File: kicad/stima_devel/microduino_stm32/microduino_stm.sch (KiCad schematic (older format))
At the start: 24 parts, among them IC1 STM32F103CBT6, IC2 LP2985, Y1 8M, Y2 32.768K

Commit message: Update schematic and testing partial routing
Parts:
- removed BUT1: KMR211GLFS, Button_Switch_SMD:SW_Push_1P1T_NO_CK_KMR2, symbol microduino_stm32-eagle-import:BUTTON-KMR241GLFS
- removed IC2: LP2985, Package_TO_SOT_SMD:SOT-23-5_HandSoldering, symbol microduino_stm32-eagle-import:LP2985
- removed KEY1: KEY-TES-018, Button_Switch_SMD:SW_SPST_EVQP7A, symbol microduino_stm32-eagle-import:KEY-TES-018
- removed LED1: BLUE, LED_SMD:LED_0805_2012Metric_Pad1.15x1.40mm_HandSolder, symbol microduino_stm32-eagle-import:LED0805
- removed R2: 1K, Resistor_SMD:R_1206_3216Metric_Pad1.30x1.75mm_HandSolder, symbol microduino_stm32-eagle-import:RESISTOR0603-RES
- removed R6: 47k, Resistor_SMD:R_1206_3216Metric_Pad1.30x1.75mm_HandSolder, symbol microduino_stm32-eagle-import:RESISTOR0603-RES
- removed R7: 10k, Resistor_SMD:R_1206_3216Metric_Pad1.30x1.75mm_HandSolder, symbol microduino_stm32-eagle-import:RESISTOR0603-RES
- removed R8, R9: 22, Resistor_SMD:R_1206_3216Metric_Pad1.30x1.75mm_HandSolder, symbol microduino_stm32-eagle-import:RESISTOR0603-RES
- removed U$2: NPN-2P, Package_TO_SOT_SMD:SOT-23-6_Handsoldering, symbol microduino_stm32-eagle-import:NPN-2P
- removed USB1: MICRO_USB, Connector_USB:USB_Micro-B_GCT_USB3076-30-A, symbol microduino_stm32-eagle-import:MICRO_USB
- removed Y2: 32.768K, Crystal:Crystal_SMD_3215-2Pin_3.2x1.5mm, symbol microduino_stm32-eagle-import:CRYSTAL-32.768K-3215
- added D2: D, Diode_SMD:D_0805_2012Metric, symbol Device:D
- added J1, J3: Conn_01x01, TestPoint:TestPoint_Pad_1.0x1.0mm, symbol Connector_Generic:Conn_01x01
- added J2: USB_B_Micro, Connector_USB:USB_Micro-B_GCT_USB3076-30-A, symbol Connector:USB_B_Micro
- added SW1: SW_Push, Button_Switch_SMD:SW_SPST_B3U-3000P, symbol Switch:SW_Push
- added SW2: SW_Push, Button_Switch_SMD:SW_Push_1P1T_NO_CK_KMR2, symbol Switch:SW_Push
- added Y2: 32.768KHz, Crystal:Crystal_SMD_EuroQuartz_EQ161-2Pin_3.2x1.5mm_HandSoldering, symbol Device:Crystal
- C1, F1: footprint Capacitor_SMD:C_1206_3216Metric_Pad1.33x1.80mm_HandSolder -> Capacitor_SMD:C_0805_2012Metric
- C6, C7: footprint Capacitor_SMD:C_1206_3216Metric_Pad1.33x1.80mm_HandSolder -> Capacitor_SMD:C_0603_1608Metric
- R1: value 1.5k -> 22; footprint Resistor_SMD:R_1206_3216Metric_Pad1.30x1.75mm_HandSolder -> Capacitor_SMD:C_0805_2012Metric
- R10, R4: footprint Resistor_SMD:R_1206_3216Metric_Pad1.30x1.75mm_HandSolder -> Capacitor_SMD:C_0805_2012Metric
- R3: value 36k -> 22; footprint Resistor_SMD:R_1206_3216Metric_Pad1.30x1.75mm_HandSolder -> Capacitor_SMD:C_0805_2012Metric
- R5: value 1k -> 1.5k; footprint Resistor_SMD:R_1206_3216Metric_Pad1.30x1.75mm_HandSolder -> Capacitor_SMD:C_0805_2012Metric
- Y1: footprint Crystal:Resonator_SMD_muRata_CSTxExxV-3Pin_3.0x1.1mm_HandSoldering -> Crystal:Resonator_SMD_muRata_CSTxExxV-3Pin_3.0x1.1mm
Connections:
- net labels removed: 32, N$13, USB_5V
- wire segments 161 -> 127
- no-connect marks 10 -> 8
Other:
- moved on the sheet: C7

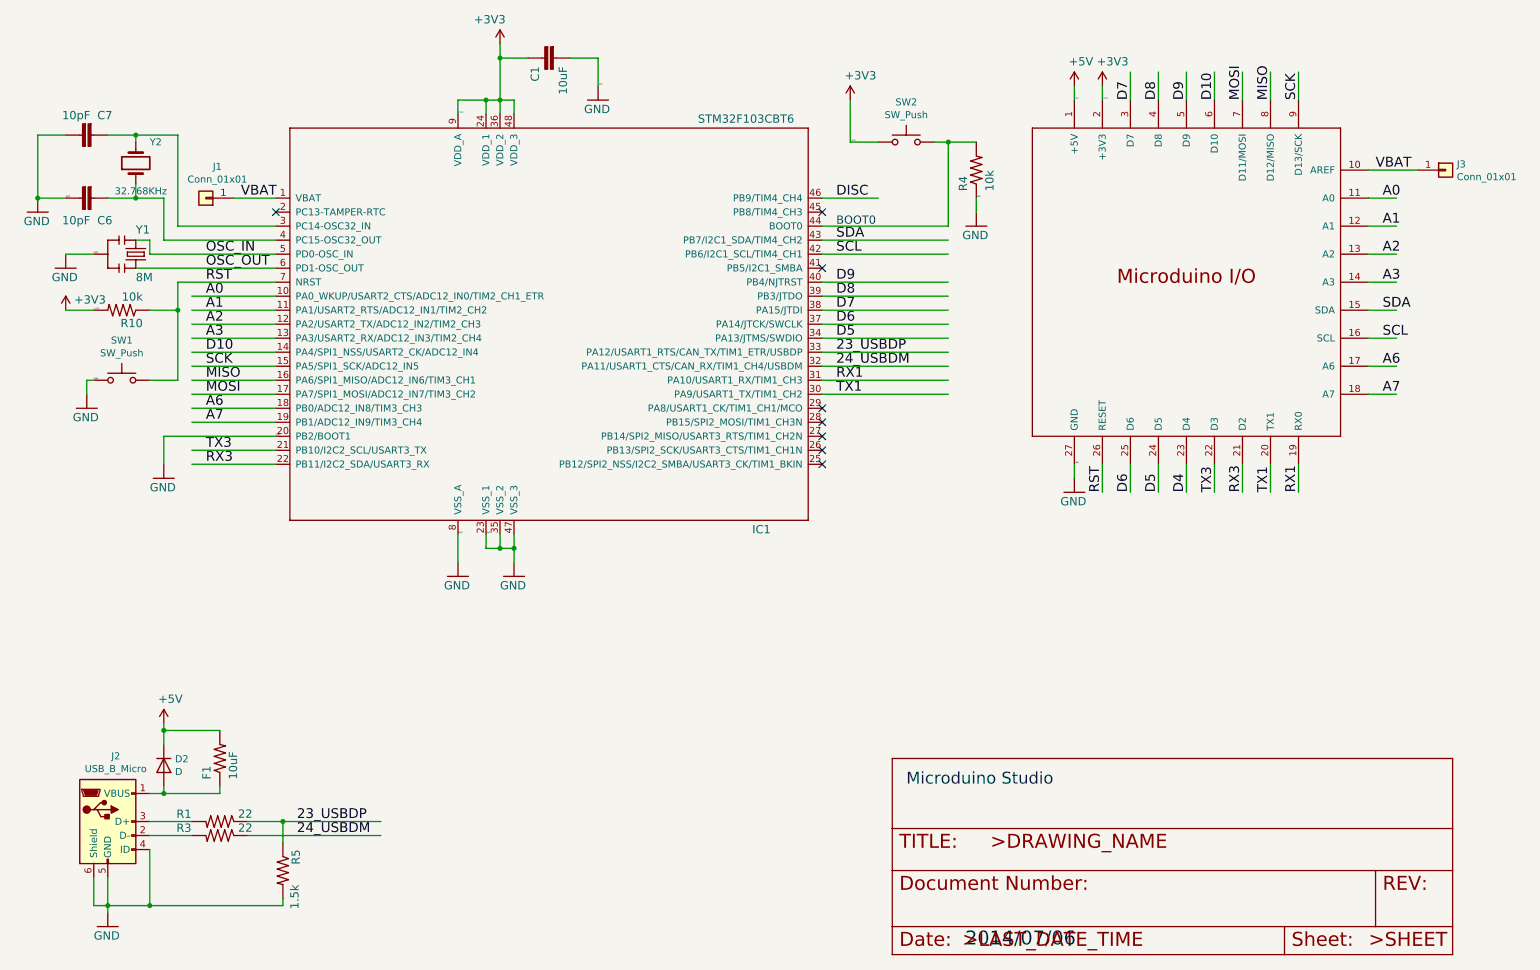
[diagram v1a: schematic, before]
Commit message: complete redraw pcb after error assignement microduino component
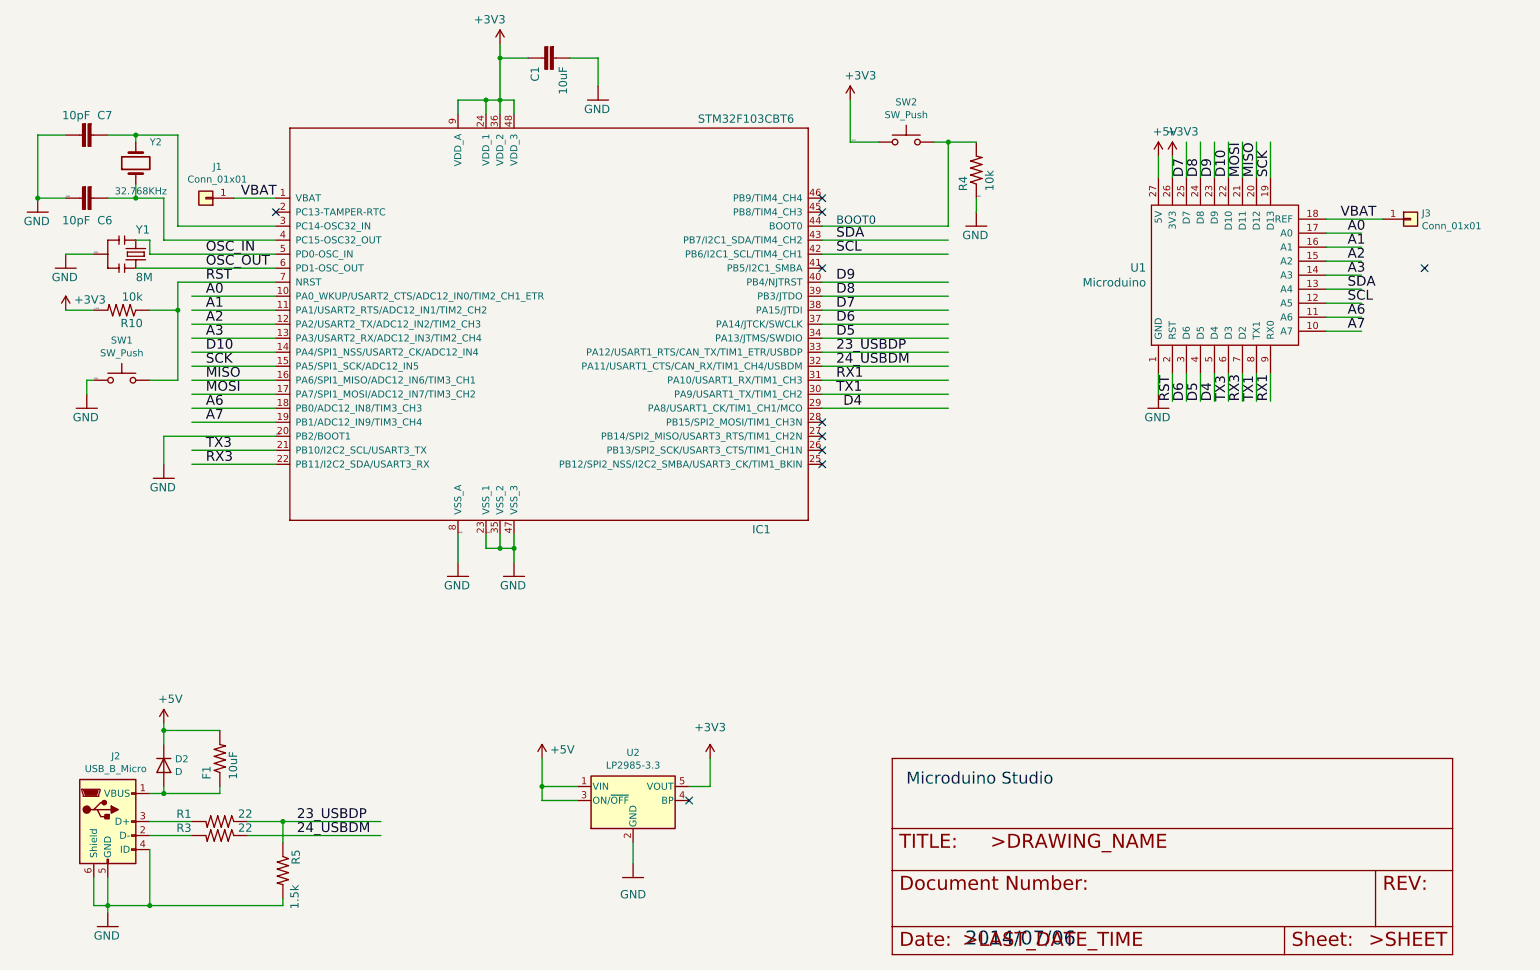
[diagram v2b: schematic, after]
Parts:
- removed U$4: MICRDUINO-PIN_NORMAL, Microduino:microduino, symbol microduino_stm32-eagle-import:MICRDUINO-PIN_NORMAL
- added U1: Microduino, Microduino:microduino, symbol microduino:Microduino
- added U2: LP2985-3.3, Package_TO_SOT_SMD:SOT-23-5, symbol Regulator_Linear:LP2985-3.3
- Y2: footprint Crystal:Crystal_SMD_EuroQuartz_EQ161-2Pin_3.2x1.5mm_HandSoldering -> Crystal:Crystal_SMD_EuroQuartz_EQ161-2Pin_3.2x1.5mm
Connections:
- net labels removed: DISC
- wire segments 127 -> 134
- no-connect marks 8 -> 10
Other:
- moved on the sheet: J3

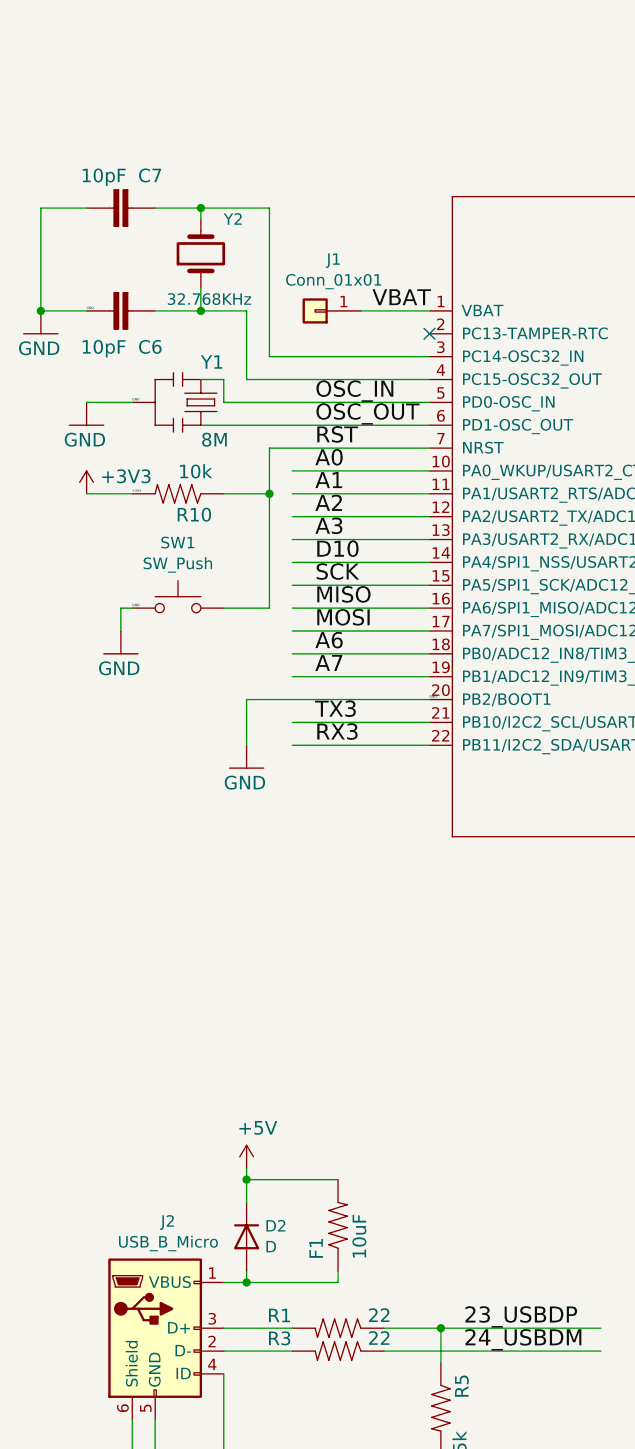
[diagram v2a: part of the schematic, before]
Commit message: update schematic
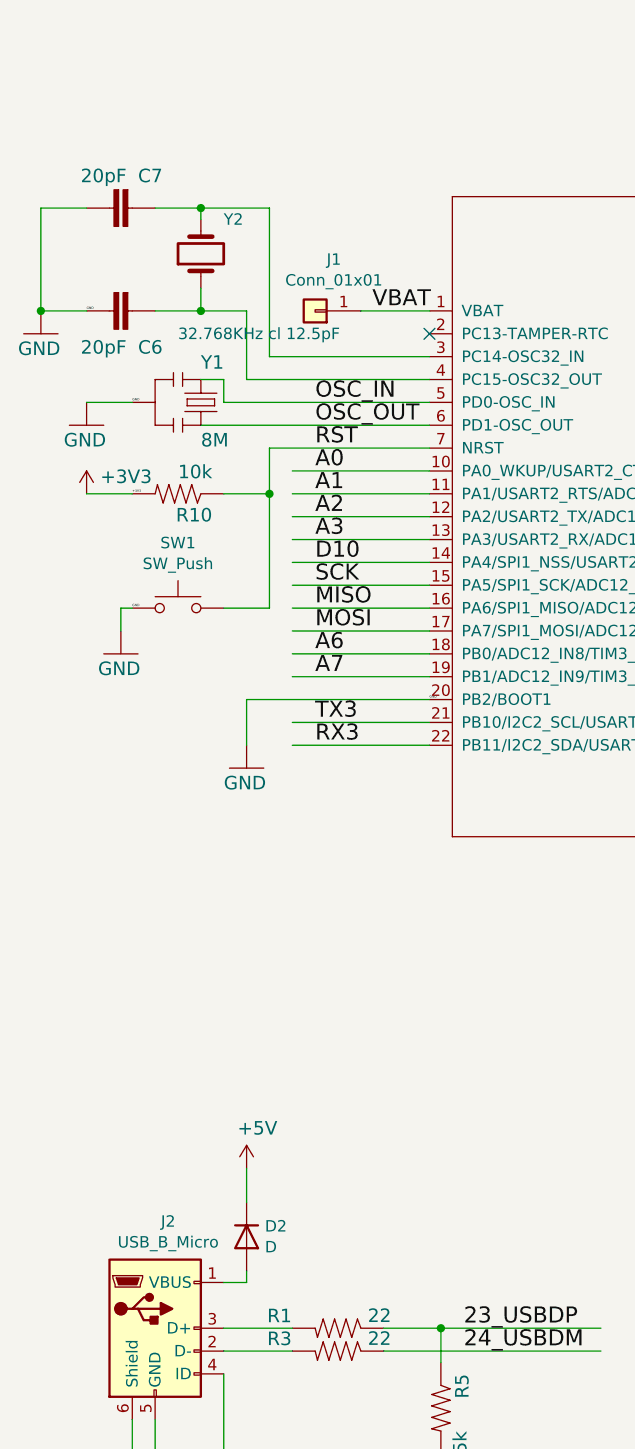
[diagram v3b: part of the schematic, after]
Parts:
- removed F1: 10uF, Capacitor_SMD:C_0805_2012Metric, symbol microduino_stm32-eagle-import:RESISTOR0805-RES
- C6, C7: value 10pF -> 20pF
- R1, R10, R3, R4, R5: footprint Capacitor_SMD:C_0805_2012Metric -> Resistor_SMD:R_0805_2012Metric
- Y2: value 32.768KHz -> 32.768KHz cl 12.5pF
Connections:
- wire segments 134 -> 130
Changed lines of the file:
@@
 F 0 "R4" H 7750 1859 59  0000 L BNN
 F 1 "10k" H 7750 1670 59  0000 L BNN
-F 2 "Capacitor_SMD:C_0805_2012Metric" H 7900 1800 50  0001 C CNN
+F 2 "Resistor_SMD:R_0805_2012Metric" H 7900 1800 50  0001 C CNN
 F 3 "" H 7900 1800 50  0001 C CNN
 	1    7900 1800
@@
 F 0 "R10" H 1650 2859 59  0000 L BNN
 F 1 "10k" H 1650 2670 59  0000 L BNN
-F 2 "Capacitor_SMD:C_0805_2012Metric" H 1800 2800 50  0001 C CNN
+F 2 "Resistor_SMD:R_0805_2012Metric" H 1800 2800 50  0001 C CNN
 F 3 "" H 1800 2800 50  0001 C CNN
 	1    1800 2800
@@
 P 1600 1550
 F 0 "C7" V 1425 1525 59  0000 R TNN
-F 1 "10pF" V 1425 1575 59  0000 L TNN
+F 1 "20pF" V 1425 1575 59  0000 L TNN
 F 2 "Capacitor_SMD:C_0603_1608Metric" H 1600 1550 50  0001 C CNN
 F 3 "" H 1600 1550 50  0001 C CNN
@@
 P 1600 2000
 F 0 "C6" V 1725 1975 59  0000 R TNN
-F 1 "10pF" V 1725 2025 59  0000 L TNN
+F 1 "20pF" V 1725 2025 59  0000 L TNN
 F 2 "Capacitor_SMD:C_0603_1608Metric" H 1600 2000 50  0001 C CNN
 F 3 "" H 1600 2000 50  0001 C CNN
@@
 P 1900 1750
 F 0 "Y2" V 2050 1650 50  0000 R CNN
-F 1 "32.768KHz" V 1700 1900 50  0000 R CNN
+F 1 "32.768KHz cl 12.5pF" V 1550 1850 50  0000 R CNN
 F 2 "Crystal:Crystal_SMD_EuroQuartz_EQ161-2Pin_3.2x1.5mm" H 1900 1750 50  0001 C CNN
 F 3 "~" H 1900 1750 50  0001 C CNN
@@
 F 0 "R5" H 2800 6859 59  0000 L BNN
 F 1 "1.5k" H 3050 6850 59  0000 L BNN
-F 2 "Capacitor_SMD:C_0805_2012Metric" H 2950 6800 50  0001 C CNN
+F 2 "Resistor_SMD:R_0805_2012Metric" H 2950 6800 50  0001 C CNN
 F 3 "" H 2950 6800 50  0001 C CNN
 	1    2950 6800
@@
 F 0 "R3" H 2810 6569 59  0000 R BNN
 F 1 "22" H 2370 6570 59  0000 R BNN
-F 2 "Capacitor_SMD:C_0805_2012Metric" H 2500 6550 50  0001 C CNN
+F 2 "Resistor_SMD:R_0805_2012Metric" H 2500 6550 50  0001 C CNN
 F 3 "" H 2500 6550 50  0001 C CNN
 	1    2500 6550
@@
 F 0 "R1" H 2810 6469 59  0000 R BNN
 F 1 "22" H 2370 6470 59  0000 R BNN
-F 2 "Capacitor_SMD:C_0805_2012Metric" H 2500 6450 50  0001 C CNN
+F 2 "Resistor_SMD:R_0805_2012Metric" H 2500 6450 50  0001 C CNN
 F 3 "" H 2500 6450 50  0001 C CNN
 	1    2500 6450
@@
 	1    0    0    -1
 $EndComp
-Wire Wire Line
-	2100 5800 2100 5900
-$Comp
-L microduino_stm32-eagle-import:RESISTOR0805-RES F1
-U 1 1 5FFF485C
-P 2500 6000
-F 0 "F1" H 2350 6059 59  0000 L BNN
-F 1 "10uF" H 2350 5870 59  0000 L BNN
-F 2 "Capacitor_SMD:C_0805_2012Metric" H 2500 6000 50  0001 C CNN
-F 3 "" H 2500 6000 50  0001 C CNN
-	1    2500 6000
-	0    -1   -1   0
-$EndComp
-Wire Wire Line
-	2100 6250 2500 6250
-Wire Wire Line
-	2500 6250 2500 6200
-Connection ~ 2100 6250
-Wire Wire Line
-	2500 5800 2100 5800
-Connection ~ 2100 5800
-Wire Wire Line
-	2100 5750 2100 5800
 Wire Wire Line
 	2000 6650 2000 7050
@@
 	1    0    0    -1
 $EndComp
+Wire Wire Line
+	2100 5750 2100 5900
 $EndSCHEMATC

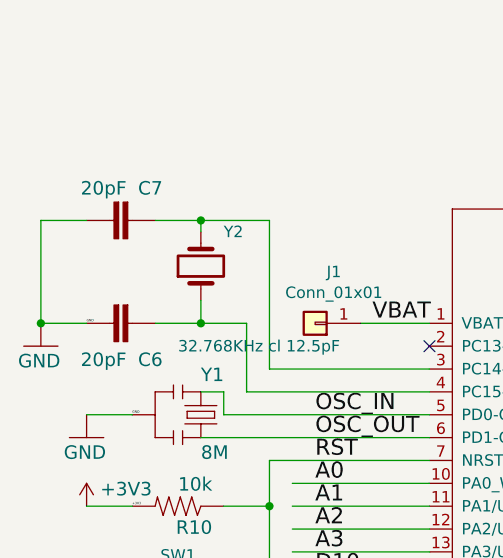
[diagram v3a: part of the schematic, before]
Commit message: update schematic 10pf c for xtal
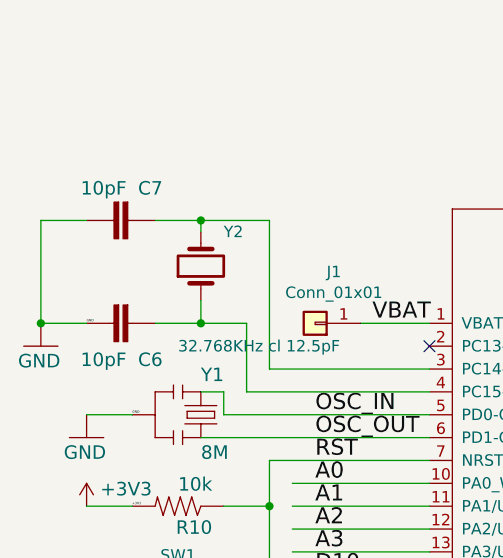
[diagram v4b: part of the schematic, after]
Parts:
- C6, C7: value 20pF -> 10pF
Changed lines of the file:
@@
 P 1600 1550
 F 0 "C7" V 1425 1525 59  0000 R TNN
-F 1 "20pF" V 1425 1575 59  0000 L TNN
+F 1 "10pF" V 1425 1575 59  0000 L TNN
 F 2 "Capacitor_SMD:C_0603_1608Metric" H 1600 1550 50  0001 C CNN
 F 3 "" H 1600 1550 50  0001 C CNN
@@
 P 1600 2000
 F 0 "C6" V 1725 1975 59  0000 R TNN
-F 1 "20pF" V 1725 2025 59  0000 L TNN
+F 1 "10pF" V 1725 2025 59  0000 L TNN
 F 2 "Capacitor_SMD:C_0603_1608Metric" H 1600 2000 50  0001 C CNN
 F 3 "" H 1600 2000 50  0001 C CNN

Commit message: change reset button switch with another footprint
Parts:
- SW1: footprint Button_Switch_SMD:SW_SPST_B3U-3000P -> Button_Switch_SMD:SW_Push_1P1T_NO_CK_KMR2
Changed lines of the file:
@@
 F 0 "SW1" H 1800 3585 50  0000 C CNN
 F 1 "SW_Push" H 1800 3494 50  0000 C CNN
-F 2 "Button_Switch_SMD:SW_SPST_B3U-3000P" H 1800 3500 50  0001 C CNN
+F 2 "Button_Switch_SMD:SW_Push_1P1T_NO_CK_KMR2" H 1800 3500 50  0001 C CNN
 F 3 "~" H 1800 3500 50  0001 C CNN
 	1    1800 3300

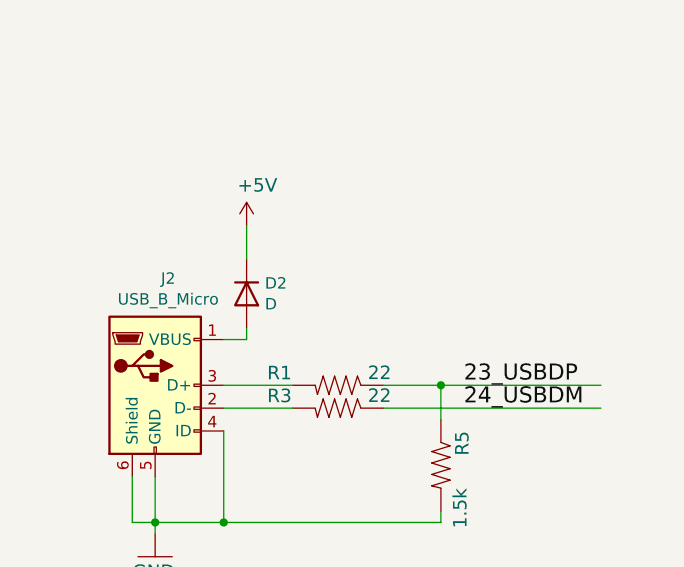
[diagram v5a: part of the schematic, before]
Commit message: change diode footprint and update pcb
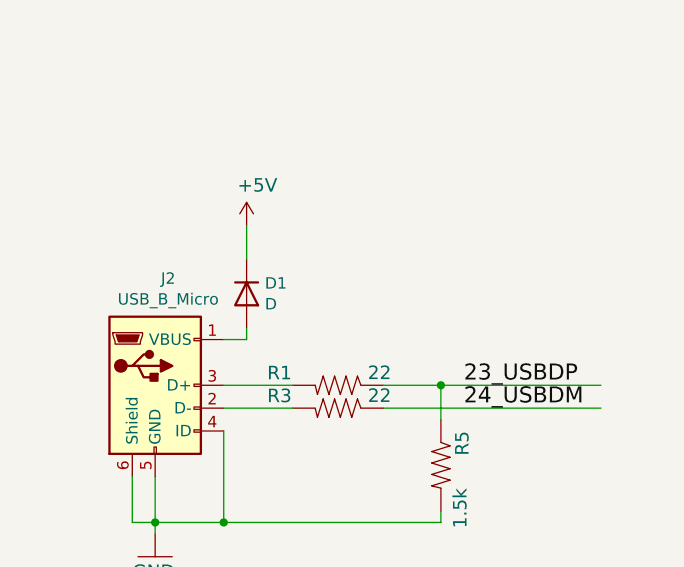
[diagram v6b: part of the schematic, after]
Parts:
- D1: renamed from D2; footprint Diode_SMD:D_0805_2012Metric -> Diode_SMD:D_SOD-123
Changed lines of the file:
@@
 Connection ~ 2950 6450
 $Comp
-L Device:D D2
+L Device:D D1
 U 1 1 600A2E09
 P 2100 6050
-F 0 "D2" V 2054 6130 50  0000 L CNN
+F 0 "D1" V 2054 6130 50  0000 L CNN
 F 1 "D" V 2145 6130 50  0000 L CNN
-F 2 "Diode_SMD:D_0805_2012Metric" H 2100 6050 50  0001 C CNN
+F 2 "Diode_SMD:D_SOD-123" H 2100 6050 50  0001 C CNN
 F 3 "~" H 2100 6050 50  0001 C CNN
 	1    2100 6050

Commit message: bug: connect R5 to Vcc
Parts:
- U1: symbol microduino:Microduino -> microduino_stm-rescue:Microduino-microduino
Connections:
- wire segments 130 -> 129
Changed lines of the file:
@@
-$EndComp
-$Comp
-L microduino_stm32-eagle-import:RESISTOR0603-RES R5
-U 1 1 5FFF4825
-P 2950 6800
-F 0 "R5" H 2800 6859 59  0000 L BNN
-F 1 "1.5k" H 3050 6850 59  0000 L BNN
-F 2 "Resistor_SMD:R_0805_2012Metric" H 2950 6800 50  0001 C CNN
-F 3 "" H 2950 6800 50  0001 C CNN
-	1    2950 6800
-	0    1    1    0
 $EndComp
 $Comp
@@
 $EndComp
 Wire Wire Line
-	2700 6450 2950 6450
-Wire Wire Line
 	1700 7100 1700 7050
 Wire Wire Line
 	1700 7050 2000 7050
-Wire Wire Line
-	2950 6450 3650 6450
-Wire Wire Line
-	2700 6550 3650 6550
-Wire Wire Line
-	2950 7050 2950 7000
-Wire Wire Line
-	2950 6450 2950 6600
-Connection ~ 2950 6450
 $Comp
 L Device:D D1
@@
 Wire Wire Line
 	2000 6650 2000 7050
-Connection ~ 2000 7050
-Wire Wire Line
-	2000 7050 2950 7050
 $Comp
 L microduino_stm32-eagle-import:DINA4_L #FRAME2
@@
 $EndComp
 $Comp
-L microduino:Microduino U1
+L microduino_stm-rescue:Microduino-microduino U1
 U 1 1 5FFE8227
 P 9400 2450
@@
 Wire Wire Line
 	2100 5750 2100 5900
+$Comp
+L microduino_stm32-eagle-import:RESISTOR0603-RES R5
+U 1 1 6020C72E
+P 2950 5950
+F 0 "R5" H 2800 6009 59  0000 L BNN
+F 1 "1.5k" H 3050 6000 59  0000 L BNN
+F 2 "Resistor_SMD:R_0805_2012Metric" H 2950 5950 50  0001 C CNN
+F 3 "" H 2950 5950 50  0001 C CNN
+	1    2950 5950
+	0    1    1    0
+$EndComp
+Wire Wire Line
+	2700 6550 3650 6550
+Wire Wire Line
+	2950 6450 3650 6450
+Wire Wire Line
+	2700 6450 2950 6450
+Connection ~ 2950 6450
+Wire Wire Line
+	2950 6150 2950 6450
+$Comp
+L microduino_stm32-eagle-import:+3V3 #P+0102
+U 1 1 6022BBF7
+P 2950 5350
+F 0 "#P+0102" H 2950 5350 50  0001 C CNN
+F 1 "+3V3" H 2950 5572 59  0000 C CNN
+F 2 "" H 2950 5350 50  0001 C CNN
+F 3 "" H 2950 5350 50  0001 C CNN
+	1    2950 5350
+	1    0    0    -1
+$EndComp
+Wire Wire Line
+	2950 5350 2950 5750
 $EndSCHEMATC
